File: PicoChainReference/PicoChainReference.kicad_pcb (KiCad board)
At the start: 4 copper layers, 68 x 34 mm, 21 parts, among them J1 RJ45, J2 RJ45, J3 +12V, J4 +5V(M), J5 I2C, J6 +5V, U1 LM78M05, U2 LM78M05, U3 LM1085, U4 PCA9615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

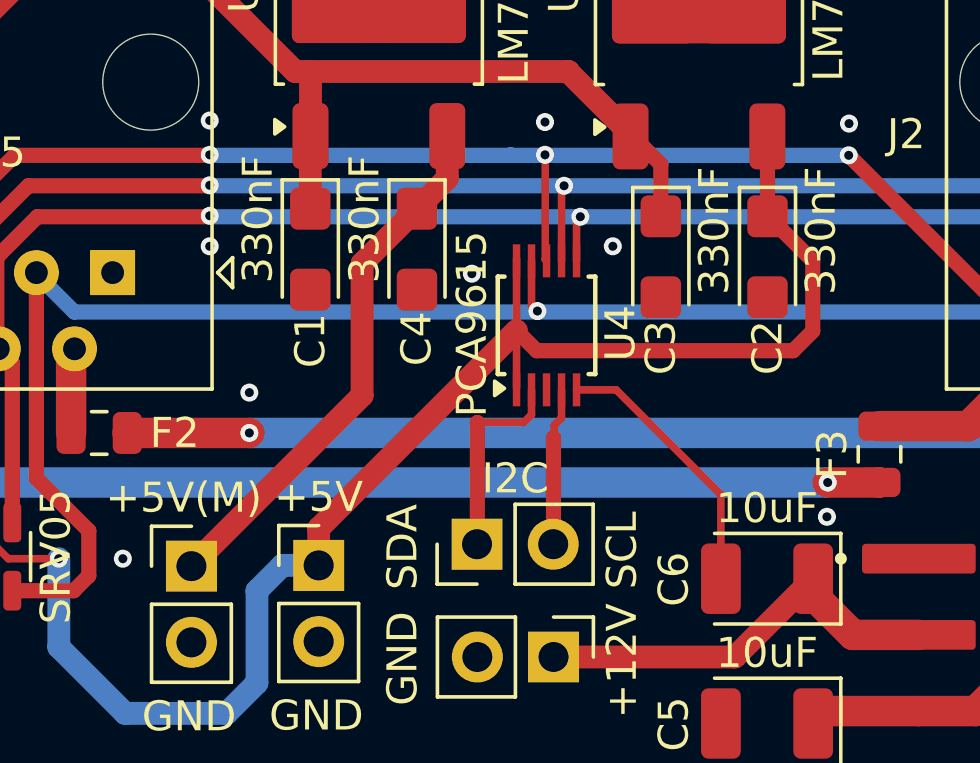
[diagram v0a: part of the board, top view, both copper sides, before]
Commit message: Added decoupling capacitors to dI2C drivers (doh)
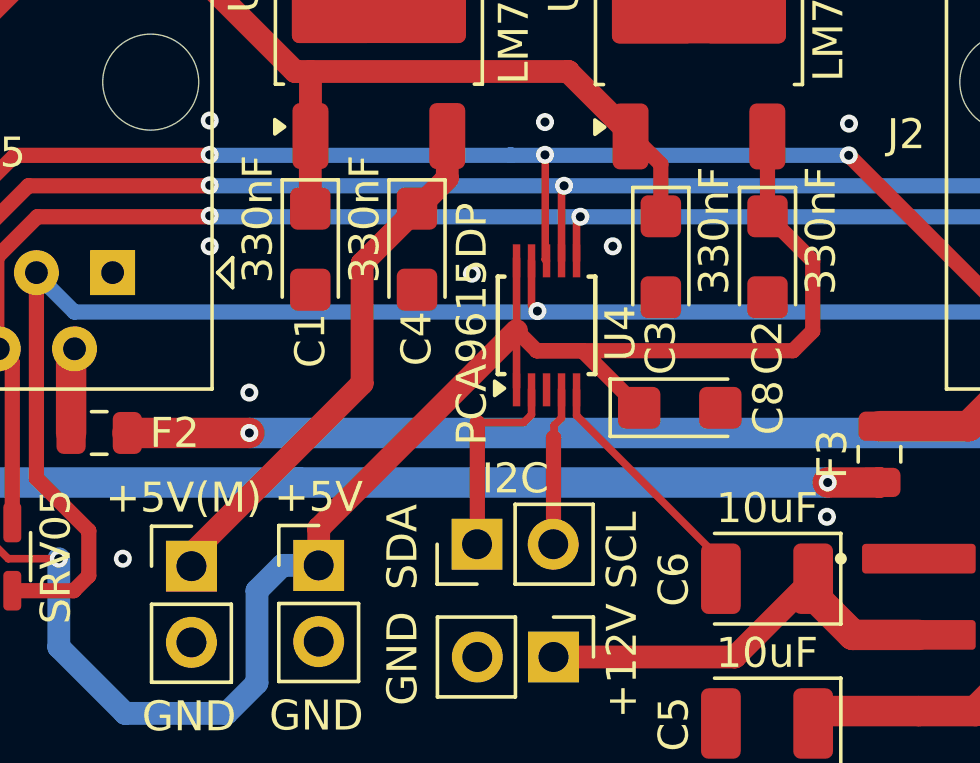
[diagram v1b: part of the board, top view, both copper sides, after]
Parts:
- added C8: 10uF, Capacitor_Tantalum_SMD:CP_EIA-3216-18_Kemet-A, F.Cu at (136.7, 85.9)
- U4: value PCA9615 -> PCA9615DP
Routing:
- net +5V: track 52.4 -> 56.6 mm
- net GND: track 9.06 -> 8.29 mm

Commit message: Finial changes before ordering first boards.
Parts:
- removed C8: 10uF, Capacitor_Tantalum_SMD:CP_EIA-3216-18_Kemet-A
- added C13: 10uF, Capacitor_SMD:C_0805_2012Metric, F.Cu at (136.3, 86.0)
